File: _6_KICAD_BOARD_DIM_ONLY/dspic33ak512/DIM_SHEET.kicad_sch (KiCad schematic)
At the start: 25 parts, among them J1 HTEC8-160-01-X-DV-A-BL-X

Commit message: feat : dim only project done
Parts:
- removed R1, R10, R11, R12, R13, R14, R15, R16, R2, R3, R4, R5, R6, R7, R8, R9: 0R, Resistor_SMD:R_0603_1608Metric, symbol Device:R_Small
- C10, C11, C6, C7: LCSC Part # (none) -> C14663
- C12, C5, C8, C9: LCSC Part # (none) -> C602037
- J1: LCSC Part # (none) -> C6571580
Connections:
- net ADC_BUS._A0: now also J1.38
- net ADC_BUS._A1: now also J1.29
- net ADC_BUS._A2: now also J1.12
- net ADC_BUS._B0: now also J1.14
- net ADC_BUS._B1: now also J1.26
- net ADC_BUS._B2: now also J1.41
- net DEBUG_BUS.MCLR: now also J1.47
- net DEBUG_BUS.PGC: now also J1.51
- net DEBUG_BUS.PGD: now also J1.49
- net GND: now also J1.SH1, J1.SH2
- net I2C_BUS.SCL: now also J1.7
- net I2C_BUS.SDA: now also J1.5
- net SPI_BUS.MISO: now also J1.34
- net SPI_BUS.MOSI: now also J1.36
- net SPI_BUS.SCLK: now also J1.32
- net SPI_BUS.SS: now also J1.30
- net SYS_BUS.BAND_SELECT: now also J1.28
- net DIM_BUS.IO16: now reaches J1.25
- net DIM_BUS.IO18: now reaches J1.27
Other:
- moved on the sheet: C10, C11, C12, C5, C6, C7, C8, C9, J1A, J1B

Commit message: feat : dim board base board 작업시작
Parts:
- C12, C5, C8, C9: LCSC Part # C602037 -> C86295
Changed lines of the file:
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@@
 			)
 		)
-		(property "LCSC Part #" "C602037"
+		(property "LCSC Part #" "C86295"
 			(at 259.08 118.11 0)
 			(effects
@@
 			)
 		)
-		(property "LCSC Part #" "C602037"
+		(property "LCSC Part #" "C86295"
 			(at 74.93 133.35 0)
 			(effects
@@
 			)
 		)
-		(property "LCSC Part #" "C602037"
+		(property "LCSC Part #" "C86295"
 			(at 190.5 118.11 0)
 			(effects
@@
 			)
 		)
-		(property "LCSC Part #" "C602037"
+		(property "LCSC Part #" "C86295"
 			(at 142.24 125.73 0)
 			(effects

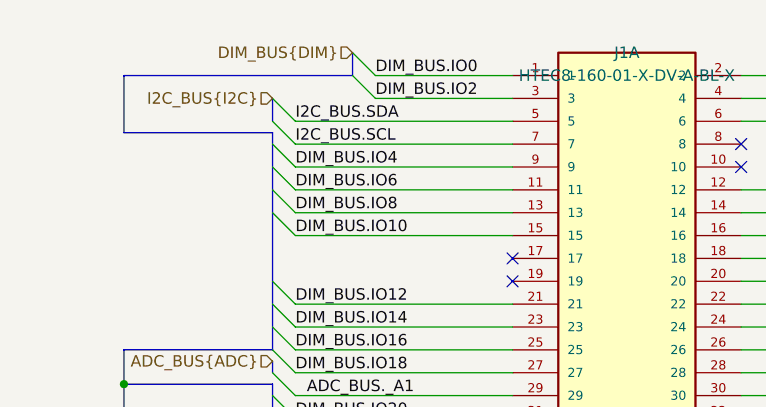
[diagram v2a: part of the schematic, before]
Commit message: feat : i2c 핀이 뒤집혀있어 fram 동작 불가 pic48 new board 또는, aux핀을 통해서 진행예정
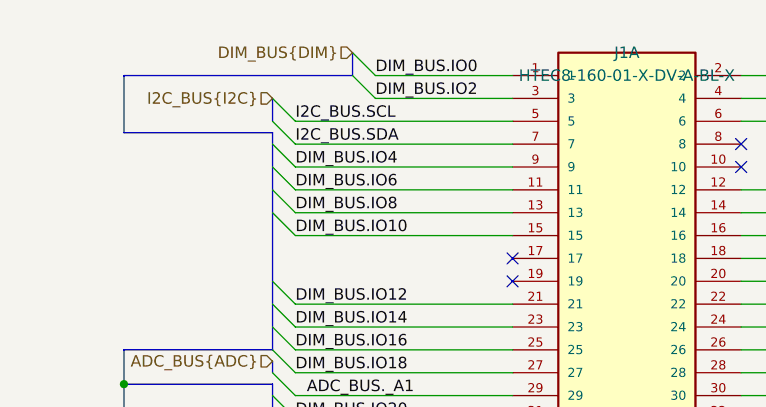
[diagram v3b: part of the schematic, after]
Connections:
- net I2C_BUS.SCL: now also J1.5; no longer J1.7
- net I2C_BUS.SDA: now also J1.7; no longer J1.5
